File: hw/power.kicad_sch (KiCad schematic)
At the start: 6 parts, among them Q1 SI2301CDS-T1-GE3, U7 XC6206P332MR

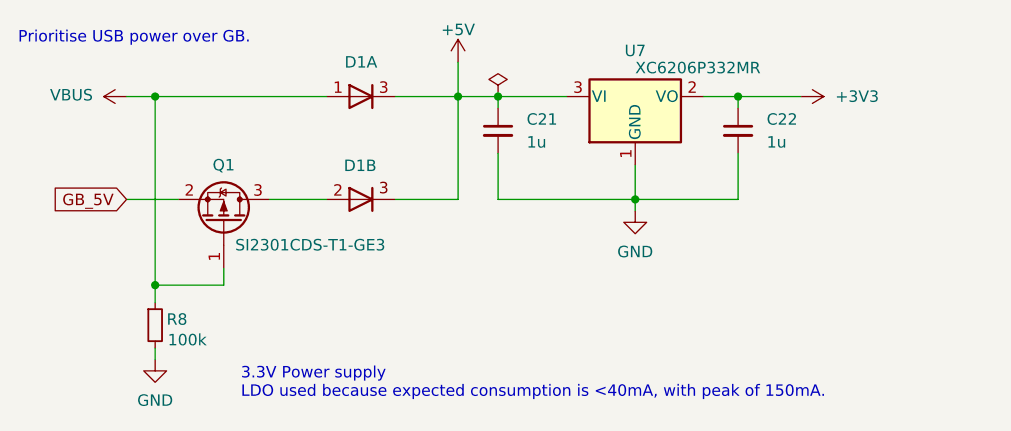
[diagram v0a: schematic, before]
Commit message: hw: multiplex Game Boy bus pins
Signed-off-by: Mahyar Koshkouei <mk@deltabeard.com>
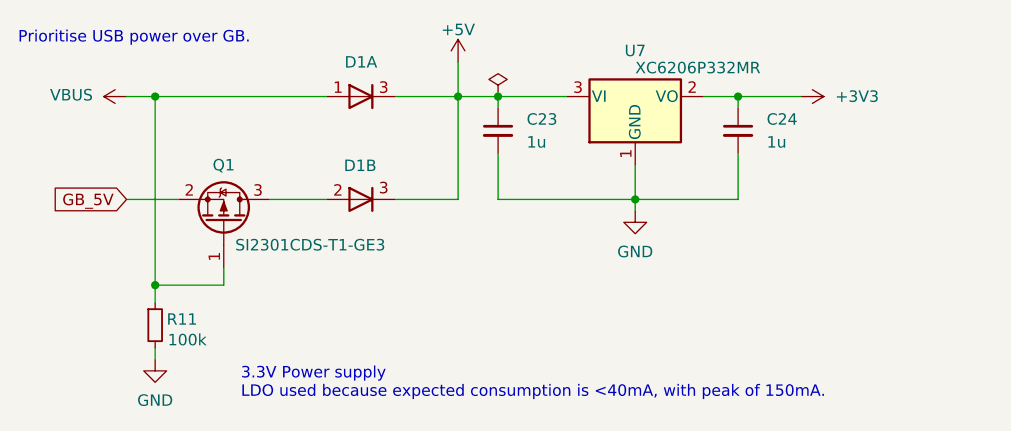
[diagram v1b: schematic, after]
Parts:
- renumbered C21 to C23, C22 to C24, R8 to R11
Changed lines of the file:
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@@
   (symbol (lib_id "power:VBUS") (at 113.665 77.47 90) (unit 1)
     (in_bom yes) (on_board yes)
-    (property "Reference" "#PWR044" (id 0) (at 117.475 77.47 0)
+    (property "Reference" "#PWR063" (id 0) (at 117.475 77.47 0)
       (effects (font (size 1.27 1.27)) hide)
     )
@@
   (symbol (lib_id "power:+5V") (at 150.495 73.66 0) (unit 1)
     (in_bom yes) (on_board yes) (fields_autoplaced)
-    (property "Reference" "#PWR046" (id 0) (at 150.495 77.47 0)
+    (property "Reference" "#PWR065" (id 0) (at 150.495 77.47 0)
       (effects (font (size 1.27 1.27)) hide)
     )
@@
   (symbol (lib_id "power:+3V3") (at 188.595 77.47 270) (unit 1)
     (in_bom yes) (on_board yes) (fields_autoplaced)
-    (property "Reference" "#PWR048" (id 0) (at 184.785 77.47 0)
+    (property "Reference" "#PWR067" (id 0) (at 184.785 77.47 0)
       (effects (font (size 1.27 1.27)) hide)
     )
@@
   (symbol (lib_id "power:GND") (at 116.84 106.68 0) (unit 1)
     (in_bom yes) (on_board yes) (fields_autoplaced)
-    (property "Reference" "#PWR045" (id 0) (at 116.84 113.03 0)
+    (property "Reference" "#PWR064" (id 0) (at 116.84 113.03 0)
       (effects (font (size 1.27 1.27)) hide)
     )
@@
   (symbol (lib_id "power:GND") (at 170.18 90.17 0) (unit 1)
     (in_bom yes) (on_board yes) (fields_autoplaced)
-    (property "Reference" "#PWR047" (id 0) (at 170.18 96.52 0)
+    (property "Reference" "#PWR066" (id 0) (at 170.18 96.52 0)
       (effects (font (size 1.27 1.27)) hide)
     )
@@
   (symbol (lib_id "Device:R_Small") (at 116.84 102.87 0) (unit 1)
     (in_bom yes) (on_board yes)
-    (property "Reference" "R8" (id 0) (at 118.11 102.2349 0)
+    (property "Reference" "R11" (id 0) (at 118.11 102.2349 0)
       (effects (font (size 1.27 1.27)) (justify left))
     )
@@
   (symbol (lib_id "Device:C_Small") (at 154.94 81.28 0) (unit 1)
     (in_bom yes) (on_board yes) (fields_autoplaced)
-    (property "Reference" "C21" (id 0) (at 158.115 80.0099 0)
+    (property "Reference" "C23" (id 0) (at 158.115 80.0099 0)
       (effects (font (size 1.27 1.27)) (justify left))
     )
@@
   (symbol (lib_id "Device:C_Small") (at 181.61 81.28 0) (unit 1)
     (in_bom yes) (on_board yes) (fields_autoplaced)
-    (property "Reference" "C22" (id 0) (at 184.785 80.0099 0)
+    (property "Reference" "C24" (id 0) (at 184.785 80.0099 0)
       (effects (font (size 1.27 1.27)) (justify left))
     )
